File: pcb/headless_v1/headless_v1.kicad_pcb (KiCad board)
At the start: 2 copper layers, 69 x 51 mm, 23 parts, among them J1 RJ10, J2 RJ10, J3 RJ10, J4 RJ10, J5 RJ10, J6 RJ10, J7 RJ10, J8 RJ10, SW1 RESET, U1 ProMicro

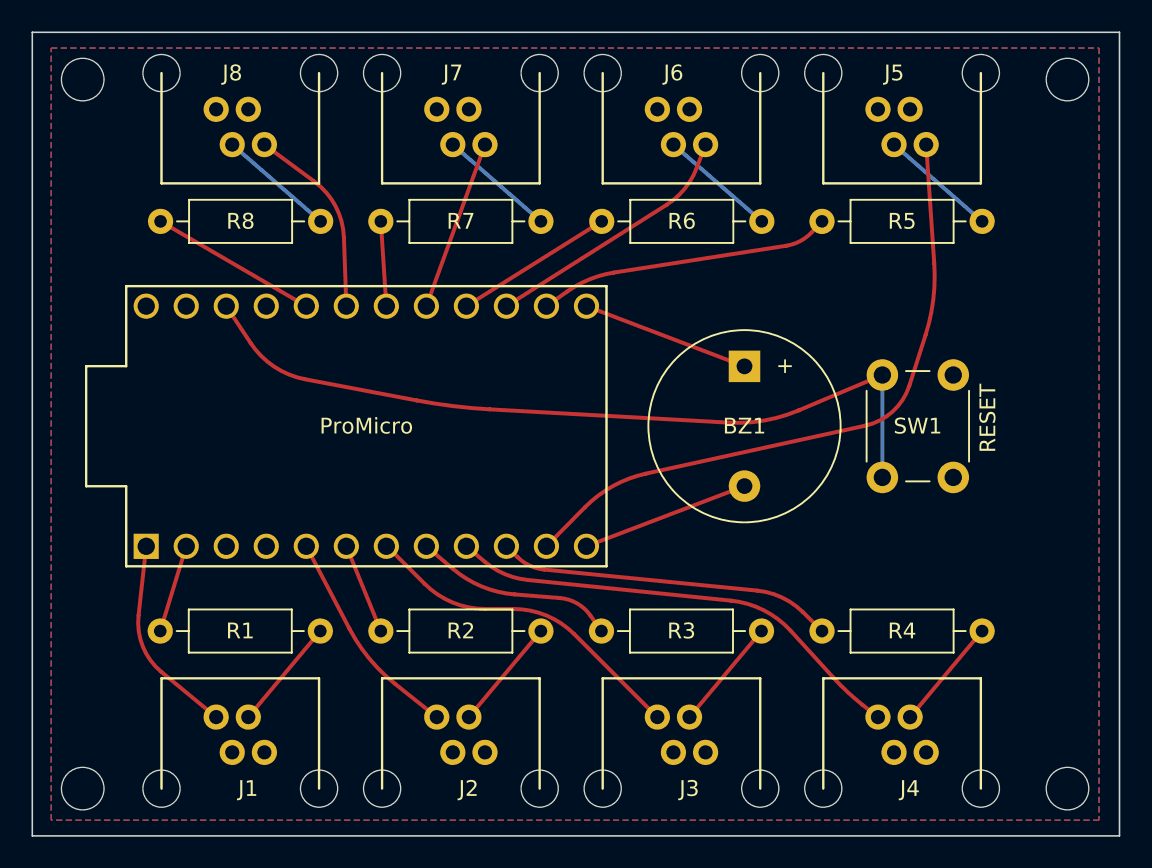
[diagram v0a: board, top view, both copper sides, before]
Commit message: Headless: minor PCB tweaks
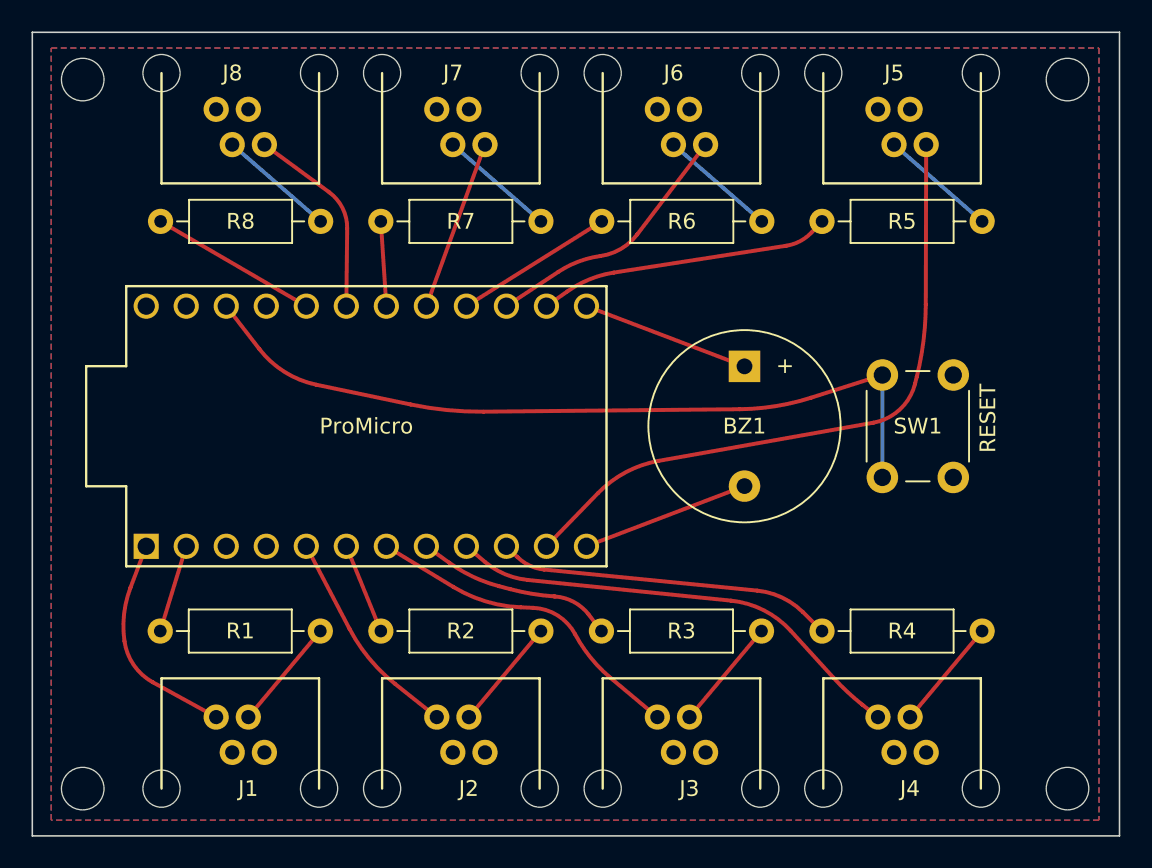
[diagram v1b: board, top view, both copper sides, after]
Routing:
- net /BUT0: track 12.9 -> 14.1 mm
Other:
- board text added: "Headless Kamaji v1.1 Ilya Strukov 2022 github.com/iley/kamaji"
- board text removed: "Headless Kamaji v1.0 Ilya Strukov 2022 github.com/iley/kamaji"
